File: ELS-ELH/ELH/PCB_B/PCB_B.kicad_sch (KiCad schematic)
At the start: 47 parts, among them J10 Conn_01x07_Pin, J11 Conn_01x08_Pin, J13 Conn_01x06_Pin, J14 TX2 3V3, J15 RX2 3V3, J16 TX2 5V, J17 RX2 5V, J18 Conn_01x06_Pin, J2 GPS Connector, J3 Conn_01x20_Pin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

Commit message: PCB B ready, PCB A layout ready
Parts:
- J3, J4: footprint Connector_PinHeader_2.54mm:PinHeader_1x20_P2.54mm_Vertical -> Connector_PinSocket_2.54mm:PinSocket_1x20_P2.54mm_Vertical
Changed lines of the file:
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@@
 			)
 		)
-		(property "Footprint" "Connector_PinHeader_2.54mm:PinHeader_1x20_P2.54mm_Vertical"
+		(property "Footprint" "Connector_PinSocket_2.54mm:PinSocket_1x20_P2.54mm_Vertical"
 			(at 146.05 44.45 0)
 			(hide yes)
@@
 			)
 		)
-		(property "Footprint" "Connector_PinHeader_2.54mm:PinHeader_1x20_P2.54mm_Vertical"
+		(property "Footprint" "Connector_PinSocket_2.54mm:PinSocket_1x20_P2.54mm_Vertical"
 			(at 107.95 44.45 0)
 			(hide yes)

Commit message: Finish PCB B
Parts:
- removed J10: Conn_01x07_Pin, Connector_PinHeader_2.54mm:PinHeader_1x07_P2.54mm_Vertical, symbol Connector:Conn_01x07_Pin
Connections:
- net D2_ESP_MAIN_3V3 is gone; now on net CS_SD_ESP_MAIN_3V3: ESP1.D2
- net D12_ESP_ESP_MAIN_3V3: no longer names the net of ESP1.D12
- net D15_ESP_MAIN_3V3: no longer names the net of ESP1.D15
- net D39_ESP_ESP_MAIN_3V3: no longer names the net of ESP1.VN (39/VN)
- net EN_ESP_MAIN_3V3: no longer names the net of ESP1.EN
- net RX0_ESP_MAIN_3V3: no longer names the net of ESP1.RX0
- net TX0_ESP_ESP_MAIN_3V3: no longer names the net of ESP1.TX0
- no-connect marks 12 -> 18
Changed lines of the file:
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@@
 	)
 	(no_connect
+		(at 44.45 24.13)
+	)
+	(no_connect
 		(at 114.3 124.46)
 	)
@@
 	)
 	(no_connect
+		(at 72.39 31.75)
+	)
+	(no_connect
 		(at 165.1 90.17)
 	)
 	(no_connect
+		(at 44.45 29.21)
+	)
+	(no_connect
 		(at 114.3 119.38)
 	)
@@
 	)
 	(no_connect
+		(at 72.39 54.61)
+	)
+	(no_connect
+		(at 44.45 52.07)
+	)
+	(no_connect
 		(at 172.72 123.19)
 	)
@@
 		(at 114.3 121.92)
 	)
+	(no_connect
+		(at 72.39 29.21)
+	)
 	(wire
 		(pts
@@
 		)
 	)
-	(label "D15_ESP_3V3"
-		(at 201.93 26.67 270)
-		(effects
-			(font
-				(size 1.27 1.27)
-			)
-			(justify right bottom)
-		)
-	)
 	(label "BUZZER_SIGNAL_ESP_MAIN_3V3"
 		(at 222.25 85.09 270)
@@
 		)
 	)
-	(label "D39_ESP_ESP_MAIN_3V3"
-		(at 44.45 29.21 180)
-		(effects
-			(font
-				(size 1.27 1.27)
-			)
-			(justify right bottom)
-		)
-	)
 	(label "R_IS_BTS7960_ESP_CTR_3V3"
 		(at 33.02 143.51 180)
@@
 		)
 	)
-	(label "RX0_ESP_3V3"
-		(at 196.85 26.67 270)
-		(effects
-			(font
-				(size 1.27 1.27)
-			)
-			(justify right bottom)
-		)
-	)
 	(label "CH_B_MOSFET_ESP_CTR_3V3"
 		(at 96.52 173.99 0)
@@
 		)
 	)
-	(label "D2_ESP_3V3"
-		(at 199.39 26.67 270)
-		(effects
-			(font
-				(size 1.27 1.27)
-			)
-			(justify right bottom)
-		)
-	)
 	(label "SCL_I2C_BUS1_ESP_MAIN_3V3"
 		(at 270.51 25.4 270)
@@
 		)
 	)
-	(label "TX0_ESP_3V3"
-		(at 194.31 26.67 270)
-		(effects
-			(font
-				(size 1.27 1.27)
-			)
-			(justify right bottom)
-		)
-	)
 	(label "LED_RED_SIGNAL_ESP_MAIN_3V3"
 		(at 44.45 54.61 180)
@@
 		)
 	)
-	(label "D12_ESP_ESP_MAIN_3V3"
-		(at 44.45 52.07 180)
-		(effects
-			(font
-				(size 1.27 1.27)
-			)
-			(justify right bottom)
-		)
-	)
 	(label "CH_C_MOSFET_ESP_MAIN_3V3"
 		(at 72.39 49.53 0)
@@
 	)
 	(label "CS_SD_ESP_MAIN_3V3"
-		(at 71.12 67.31 0)
+		(at 72.39 52.07 0)
 		(effects
 			(font
@@
 		)
 	)
-	(label "D12_ESP_3V3"
-		(at 191.77 26.67 270)
-		(effects
-			(font
-				(size 1.27 1.27)
-			)
-			(justify right bottom)
-		)
-	)
 	(label "L_IS_BTS7960_ESP_CTR_3V3"
 		(at 35.56 156.21 180)
@@
 		)
 	)
-	(label "EN_ESP_MAIN_3V3"
-		(at 44.45 24.13 180)
-		(effects
-			(font
-				(size 1.27 1.27)
-			)
-			(justify right bottom)
-		)
-	)
 	(label "RPWM_BTS7960_ESP_CTR_3V3"
 		(at 68.58 168.91 180)
@@
 		)
 	)
-	(label "D15_ESP_MAIN_3V3"
-		(at 72.39 54.61 0)
-		(effects
-			(font
-				(size 1.27 1.27)
-			)
-			(justify left bottom)
-		)
-	)
-	(label "RX0_ESP_MAIN_3V3"
-		(at 72.39 31.75 0)
-		(effects
-			(font
-				(size 1.27 1.27)
-			)
-			(justify left bottom)
-		)
-	)
 	(label "RX_UART_BUS2_5V"
 		(at 35.56 88.9 180)
@@
 		)
 	)
-	(label "EN_ESP_3V3"
-		(at 186.69 26.67 270)
-		(effects
-			(font
-				(size 1.27 1.27)
-			)
-			(justify right bottom)
-		)
-	)
 	(label "CH_D_MOSFET_ESP_MAIN_3V3"
 		(at 116.84 41.91 0)
@@
 		)
 	)
-	(label "D39_ESP_3V3"
-		(at 189.23 26.67 270)
-		(effects
-			(font
-				(size 1.27 1.27)
-			)
-			(justify right bottom)
-		)
-	)
 	(label "R_EN_BTS7960_ESP_CTR_3V3"
 		(at 68.58 173.99 180)
@@
 		)
 	)
-	(label "D2_ESP_MAIN_3V3"
-		(at 72.39 52.07 0)
-		(effects
-			(font
-				(size 1.27 1.27)
-			)
-			(justify left bottom)
-		)
-	)
-	(label "TX0_ESP_ESP_MAIN_3V3"
-		(at 72.39 29.21 0)
-		(effects
-			(font
-				(size 1.27 1.27)
-			)
-			(justify left bottom)
-		)
-	)
 	(label "SCK_SPI_BUS1_ESP_MAIN_3V3"
 		(at 44.45 125.73 180)
@@
 					(unit 1)
 				)
-			)
-		)
-	)
-	(symbol
-		(lib_id "Connector:Conn_01x07_Pin")
-		(at 194.31 21.59 270)
-		(unit 1)
-		(body_style 1)
-		(exclude_from_sim no)
-		(in_bom yes)
-		(on_board yes)
-		(in_pos_files yes)
-		(dnp no)
-		(fields_autoplaced yes)
-		(property "Reference" "J10"
-			(at 194.31 17.78 90)
-			(show_name no)
-			(do_not_autoplace no)
-			(effects
-				(font
-					(size 1.27 1.27)
-				)
-			)
-		)
-		(property "Value" "Conn_01x07_Pin"
-			(at 194.31 20.32 90)
-			(show_name no)
-			(do_not_autoplace no)
-			(effects
-				(font
-					(size 1.27 1.27)
-				)
-			)
-		)
-		(property "Footprint" "Connector_PinHeader_2.54mm:PinHeader_1x07_P2.54mm_Vertical"
-			(at 194.31 21.59 0)
-			(hide yes)
-			(show_name no)
-			(do_not_autoplace no)
-			(effects
-				(font
-					(size 1.27 1.27)
-				)
-			)
-		)
-		(property "Datasheet" ""
-			(at 194.31 21.59 0)
-			(hide yes)
-			(show_name no)
-			(do_not_autoplace no)
-			(effects
-				(font
-					(size 1.27 1.27)
-				)
-			)
-		)
-		(property "Description" "Generic connector, single row, 01x07, script generated"
-			(at 194.31 21.59 0)
-			(hide yes)
-			(show_name no)
-			(do_not_autoplace no)
-			(effects
-				(font
-					(size 1.27 1.27)
-				)
-			)
-		)
-		(pin "7"
-		)
-		(pin "3"
-		)
-		(pin "4"
-		)
-		(pin "5"
-		)
-		(pin "6"
-		)
-		(pin "1"
-		)
-		(pin "2"
-		)
-		(instances
-			(project "PCB_B"
-				(path "/8ce3d015-2fa7-4d89-b6ca-9a5bdbe9d762"
-					(reference "J10")
-					(unit 1)
-				)

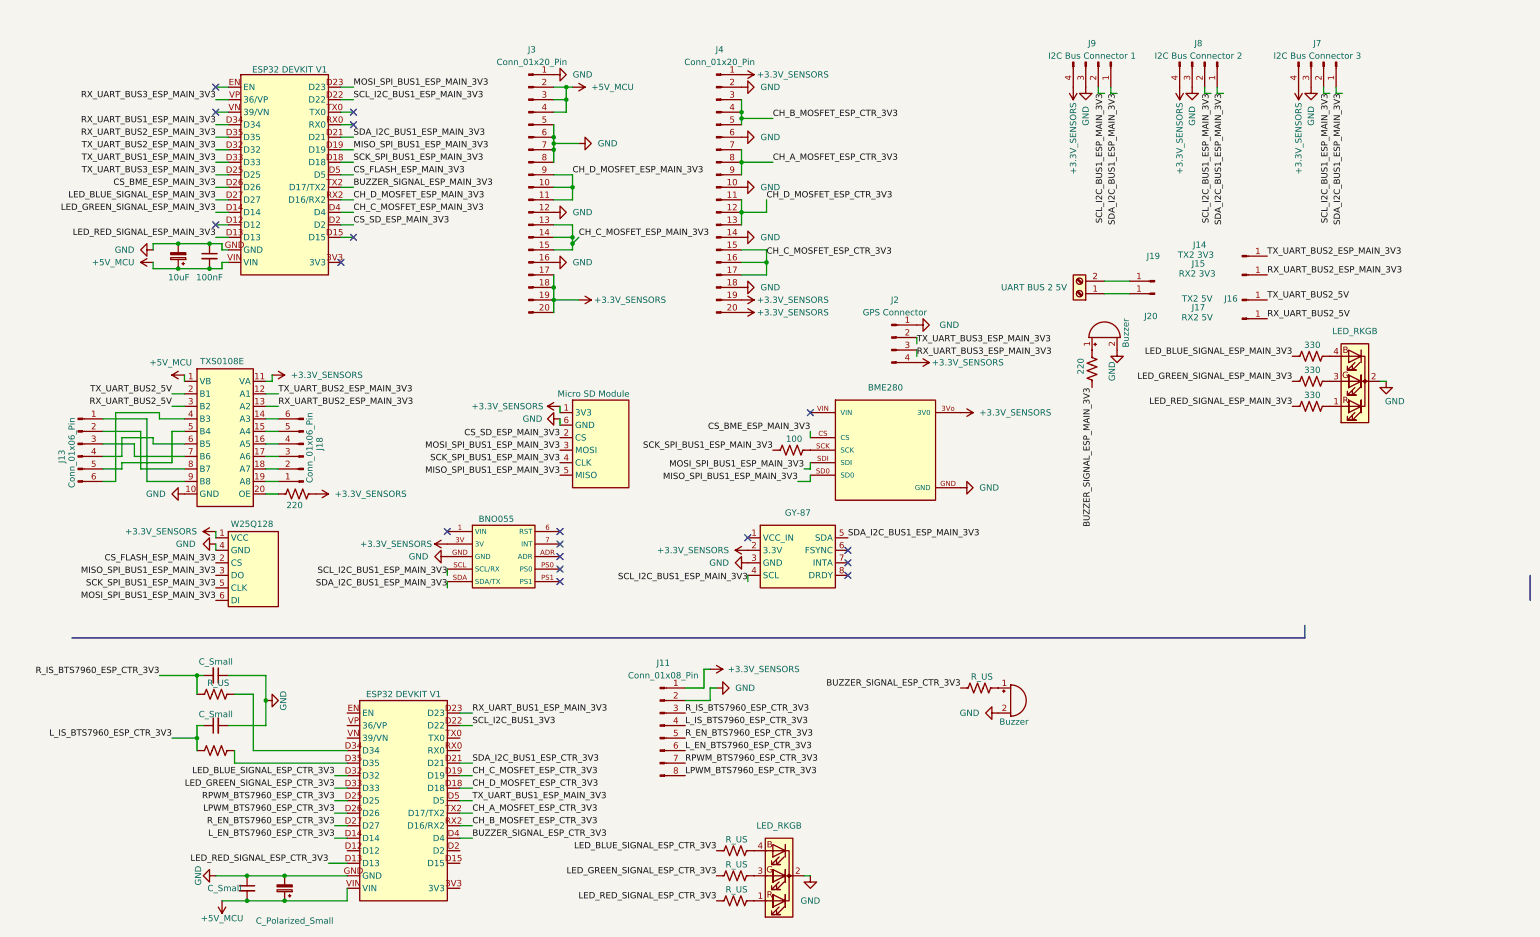
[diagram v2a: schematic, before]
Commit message: Solve DRC problems with B
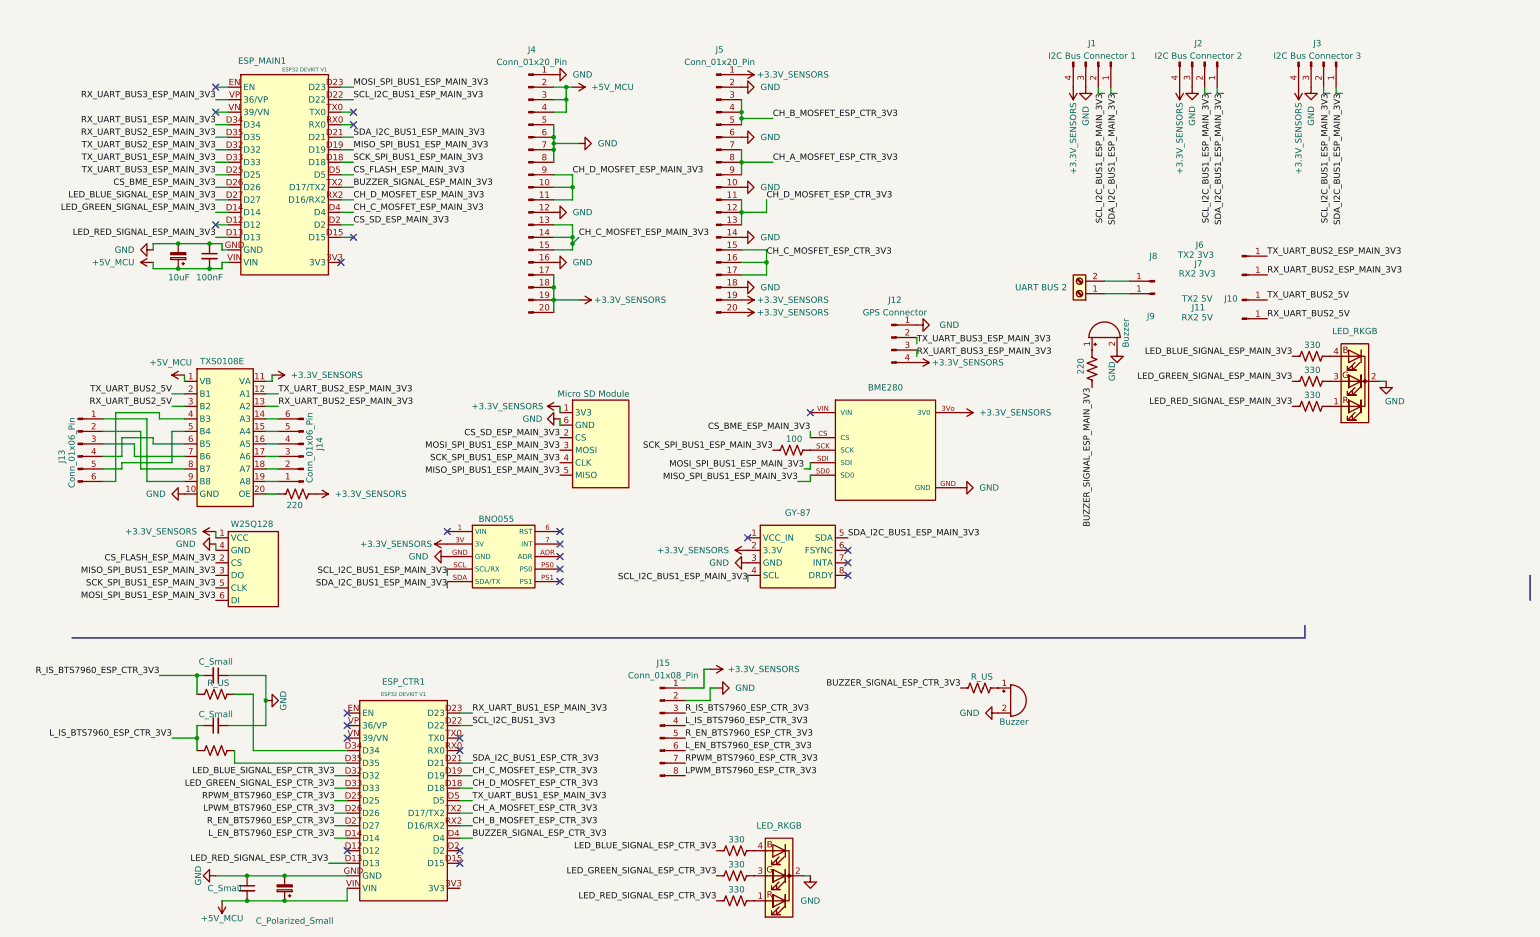
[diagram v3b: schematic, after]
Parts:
- BZ1, BZ2: footprint Buzzer_Beeper:Buzzer_12x9.5RM7.6 -> (none)
- Bornera1: renamed from Bornera7; value UART BUS 2 5V -> UART BUS 2; footprint ELH_Library:Bornera 2P -> (none)
- C1: renamed from C13; footprint Capacitor_THT:CP_Radial_D5.0mm_P2.50mm -> (none)
- C2: footprint Capacitor_THT:C_Disc_D5.0mm_W2.5mm_P5.00mm -> (none)
- C3: renamed from C1; footprint Capacitor_THT:C_Disc_D5.0mm_W2.5mm_P5.00mm -> (none)
- C4: renamed from C3; footprint Capacitor_THT:C_Disc_D5.0mm_W2.5mm_P5.00mm -> (none)
- C5: renamed from C4; footprint Capacitor_THT:C_Disc_D5.0mm_W2.5mm_P5.00mm -> (none)
- C6: renamed from C5; footprint Capacitor_THT:CP_Radial_D5.0mm_P2.50mm -> (none)
- Converter1: footprint ELH_Library:TXS0108E -> (none)
- D1: renamed from D10; footprint ELH_Library:LED RGB -> (none)
- D2: renamed from D1; footprint LED_THT:LED_D5.0mm-4_RGB_Staggered_Pins -> (none)
- J1: renamed from J9; footprint Connector_PinHeader_2.54mm:PinHeader_1x04_P2.54mm_Vertical -> (none)
- J10: renamed from J16; footprint Connector_PinSocket_2.54mm:PinSocket_1x01_P2.54mm_Vertical -> (none)
- J11: renamed from J17; footprint Connector_PinSocket_2.54mm:PinSocket_1x01_P2.54mm_Vertical -> (none)
- J12: renamed from J2; footprint Connector_PinSocket_2.54mm:PinSocket_1x04_P2.54mm_Vertical -> (none)
- J13: footprint Connector_PinHeader_2.54mm:PinHeader_1x06_P2.54mm_Vertical -> (none)
- J14: renamed from J18; footprint Connector_PinHeader_2.54mm:PinHeader_1x06_P2.54mm_Vertical -> (none)
- J15: renamed from J11; footprint Connector_PinSocket_2.54mm:PinSocket_1x08_P2.54mm_Vertical -> (none)
- J2: renamed from J8; footprint Connector_PinHeader_2.54mm:PinHeader_1x04_P2.54mm_Vertical -> (none)
- J3: renamed from J7; footprint Connector_PinHeader_2.54mm:PinHeader_1x04_P2.54mm_Vertical -> (none)
- J4: renamed from J3; footprint Connector_PinSocket_2.54mm:PinSocket_1x20_P2.54mm_Vertical -> (none)
- J5: renamed from J4; footprint Connector_PinSocket_2.54mm:PinSocket_1x20_P2.54mm_Vertical -> (none)
- J6: renamed from J14; footprint Connector_PinSocket_2.54mm:PinSocket_1x01_P2.54mm_Vertical -> (none)
- J7: renamed from J15; footprint Connector_PinSocket_2.54mm:PinSocket_1x01_P2.54mm_Vertical -> (none)
- J8: renamed from J19; footprint Connector_PinSocket_2.54mm:PinSocket_1x01_P2.54mm_Vertical -> (none)
- J9: renamed from J20; footprint Connector_PinSocket_2.54mm:PinSocket_1x01_P2.54mm_Vertical -> (none)
- R1: renamed from R7; footprint Resistor_THT:R_Axial_DIN0207_L6.3mm_D2.5mm_P7.62mm_Horizontal -> (none)
- R10: renamed from R6; value R_US -> 330; footprint Resistor_THT:R_Axial_DIN0207_L6.3mm_D2.5mm_P7.62mm_Horizontal -> (none)
- R11: renamed from R8; value R_US -> 330; footprint Resistor_THT:R_Axial_DIN0207_L6.3mm_D2.5mm_P7.62mm_Horizontal -> (none)
- R12: renamed from R9; value R_US -> 330; footprint Resistor_THT:R_Axial_DIN0207_L6.3mm_D2.5mm_P7.62mm_Horizontal -> (none)
- R2: renamed from R12; footprint Resistor_THT:R_Axial_DIN0207_L6.3mm_D2.5mm_P7.62mm_Horizontal -> (none)
- R3: renamed from R5; footprint Resistor_THT:R_Axial_DIN0207_L6.3mm_D2.5mm_P7.62mm_Horizontal -> (none)
- R4: footprint Resistor_THT:R_Axial_DIN0207_L6.3mm_D2.5mm_P7.62mm_Horizontal -> (none)
- R5: renamed from R13; footprint Resistor_THT:R_Axial_DIN0207_L6.3mm_D2.5mm_P7.62mm_Horizontal -> (none)
- R6: renamed from R14; footprint Resistor_THT:R_Axial_DIN0207_L6.3mm_D2.5mm_P7.62mm_Horizontal -> (none)
- R7: renamed from R3; footprint Resistor_THT:R_Axial_DIN0207_L6.3mm_D2.5mm_P7.62mm_Horizontal -> (none)
- R8: renamed from R1; footprint Resistor_THT:R_Axial_DIN0207_L6.3mm_D2.5mm_P7.62mm_Horizontal -> (none)
- R9: renamed from R2; footprint Resistor_THT:R_Axial_DIN0207_L6.3mm_D2.5mm_P7.62mm_Horizontal -> (none)
- renumbered BME2 to BME1, ESP2 to ESP_CTR1, ESP1 to ESP_MAIN1, IMU3 to IMU1
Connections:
- no-connect marks 18 -> 26

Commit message: Update almost finished
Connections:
- net CH_A_MOSFET_ESP_CTR_3V3: now also ESP_CTR1.D19, J5.15 (Pin_15), J5.16 (Pin_16), J5.17 (Pin_17); no longer ESP_CTR1.TX2 (D17/TX2), J5.7 (Pin_7), J5.8 (Pin_8), J5.9 (Pin_9)
- net CH_C_MOSFET_ESP_CTR_3V3: now also ESP_CTR1.TX2 (D17/TX2), J5.7 (Pin_7), J5.8 (Pin_8), J5.9 (Pin_9); no longer ESP_CTR1.D19, J5.15 (Pin_15), J5.16 (Pin_16), J5.17 (Pin_17)
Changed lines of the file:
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@@
+		)
+	)
+	(label "CH_C_MOSFET_ESP_CTR_3V3"
+		(at 96.52 171.45 0)
+		(effects
+			(font
+				(size 1.27 1.27)
+			)
+			(justify left bottom)
 		)
 	)
@@
 		)
 	)
-	(label "CH_A_MOSFET_ESP_CTR_3V3"
-		(at 96.52 171.45 0)
-		(effects
-			(font
-				(size 1.27 1.27)
-			)
-			(justify left bottom)
-		)
-	)
 	(label "CH_D_MOSFET_ESP_CTR_3V3"
 		(at 96.52 166.37 0)
@@
 	)
 	(label "CH_C_MOSFET_ESP_CTR_3V3"
-		(at 96.52 163.83 0)
-		(effects
-			(font
-				(size 1.27 1.27)
-			)
-			(justify left bottom)
-		)
-	)
-	(label "CH_C_MOSFET_ESP_CTR_3V3"
-		(at 156.21 58.42 0)
+		(at 157.48 39.37 0)
 		(effects
 			(font
@@
 		)
 	)
-	(label "CH_A_MOSFET_ESP_CTR_3V3"
-		(at 157.48 39.37 0)
-		(effects
-			(font
-				(size 1.27 1.27)
-			)
-			(justify left bottom)
-		)
-	)
 	(label "CS_SD_ESP_MAIN_3V3"
 		(at 72.39 52.07 0)
@@
 		)
 	)
+	(label "CH_A_MOSFET_ESP_CTR_3V3"
+		(at 96.52 163.83 0)
+		(effects
+			(font
+				(size 1.27 1.27)
+			)
+			(justify left bottom)
+		)
+	)
 	(label "SCK_SPI_BUS1_ESP_MAIN_3V3"
 		(at 44.45 125.73 180)
@@
 		)
 	)
+	(label "CH_A_MOSFET_ESP_CTR_3V3"
+		(at 156.21 59.69 0)
+		(effects
+			(font
+				(size 1.27 1.27)
+			)
+			(justify left bottom)
+		)
+	)

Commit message: Finished the manufacture
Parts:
- removed J10: TX2 5V, symbol Connector:Conn_01x01_Pin
- removed J11: RX2 5V, symbol Connector:Conn_01x01_Pin
- removed J6: TX2 3V3, symbol Connector:Conn_01x01_Pin
- removed J7: RX2 3V3, symbol Connector:Conn_01x01_Pin
- removed J8, J9: (no value), symbol Connector:Conn_01x01_Pin
- added J16: Conn_02x04_Odd_Even, Connector_PinHeader_2.54mm:PinHeader_2x04_P2.54mm_Vertical, symbol Connector_Generic:Conn_02x04_Odd_Even
- added J6: Conn_01x02_Pin, Connector_PinHeader_2.54mm:PinHeader_1x02_P2.54mm_Vertical, symbol Connector:Conn_01x02_Pin
- C3, C4: value C_Small -> ???
- C5: value C_Small -> 100nF
- C6: value C_Polarized_Small -> 10uF
- R7: value R_US -> 220
- R8, R9: value R_US -> ???
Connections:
- net +3.3V_SENSORS: now also J6.2 (Pin_2)
- net RX_UART_BUS2_5V: now also J16.1 (Pin_1)
- net RX_UART_BUS2_ESP_MAIN_3V3: now also J16.4 (Pin_4)
- net TX_UART_BUS2_5V: now also J16.7 (Pin_7)
- net TX_UART_BUS2_ESP_MAIN_3V3: now also J16.6 (Pin_6)
- net at Bornera1.2 (Pin_2): now also J16.5 (Pin_5)
- net +3.3V_ESP_MAIN: now reaches ESP_MAIN1.3V3
- net +3.3V_ESP_MAIN: now also J6.1 (Pin_1)
- net at Bornera1.1 (Pin_1): now also J16.3 (Pin_3)
- no-connect marks 26 -> 25
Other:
- moved on the sheet: J1, J2, J3
